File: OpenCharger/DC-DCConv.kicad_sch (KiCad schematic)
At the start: 10 parts, among them Q5 IPT015N10N5, Q6 IPT015N10N5, Q7 IPT015N10N5, Q9 IPT015N10N5, U4 IRS25606S

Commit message: updated
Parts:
- removed C12, C13, C9: 56uF, Capacitor_THT:CP_Radial_D40.0mm_P10.00mm_SnapIn, symbol Device:C_Polarized_US
- removed U4: IRS25606S, Package_SO:SOIC-8_3.9x4.9mm_P1.27mm, symbol Driver_FET:IRS25606S
- added C10, C15, C16, C6, C8: 100uF, Capacitor_THT:CP_Radial_D16.0mm_P7.50mm, symbol Device:C_Polarized_US
- added Q18, Q19, Q20, Q21, Q22, Q23, Q24, Q25: IPT015N10N5, Package_TO_SOT_SMD:Infineon_PG-HSOF-8-1, symbol Transistor_FET:IPT015N10N5
- C14: value 56uF -> 100uF; footprint Capacitor_THT:CP_Radial_D40.0mm_P10.00mm_SnapIn -> Capacitor_THT:CP_Radial_D16.0mm_P7.50mm
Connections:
- net V_{in}-: now also C10.2, C15.2, C16.2, C6.2, C8.2
- net V_{out}+: now also C10.1, C15.1, C16.1, C6.1, C8.1, Q25.3 (D); no longer Q9.3 (D)
- net BOOST_SG0: now reaches Q7.1 (G)
- net L-: now reaches L1.2, Q9.2 (S)
- net L-: now also Q22.3 (D); no longer Q7.3 (D)
- net BUCK_DG0: now reaches Q6.1 (G)
- net BOOST_DG0: now reaches Q9.1 (G)
- net BUCK_SG2: now reaches Q5.1 (G)
- new net BOOST_DG1: Q24.1 (G)
- new net BOOST_DG2: Q25.1 (G)
- new net BOOST_DS1: Q24.2 (S), Q9.3 (D)
- new net BOOST_DS2: Q24.3 (D), Q25.2 (S)
- new net BOOST_SG1: Q23.1 (G)
- new net BOOST_SG2: Q22.1 (G)
- new net BOOST_SS1: Q23.2 (S), Q7.3 (D)
- new net BOOST_SS2: Q22.2 (S), Q23.3 (D)
- new net BUCK_DG1: Q21.1 (G)
- new net BUCK_DG2: Q20.1 (G)
- new net BUCK_DS1: Q21.2 (S), Q6.3 (D)
- new net BUCK_DS2: Q20.2 (S), Q21.3 (D)
- new net BUCK_SG0: Q19.1 (G)
- new net BUCK_SG1: Q18.1 (G)
- new net BUCK_SS1: Q18.2 (S), Q19.3 (D)
- new net BUCK_SS2: Q18.3 (D), Q5.2 (S)
- new net L+: L1.1, Q19.2 (S), Q20.3 (D)
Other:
- added sheet DC-DC Converter Gate Driver (DCDCGateDrivers.kicad_sch)
- moved on the sheet: L1, Q5, Q6, Q7, Q9

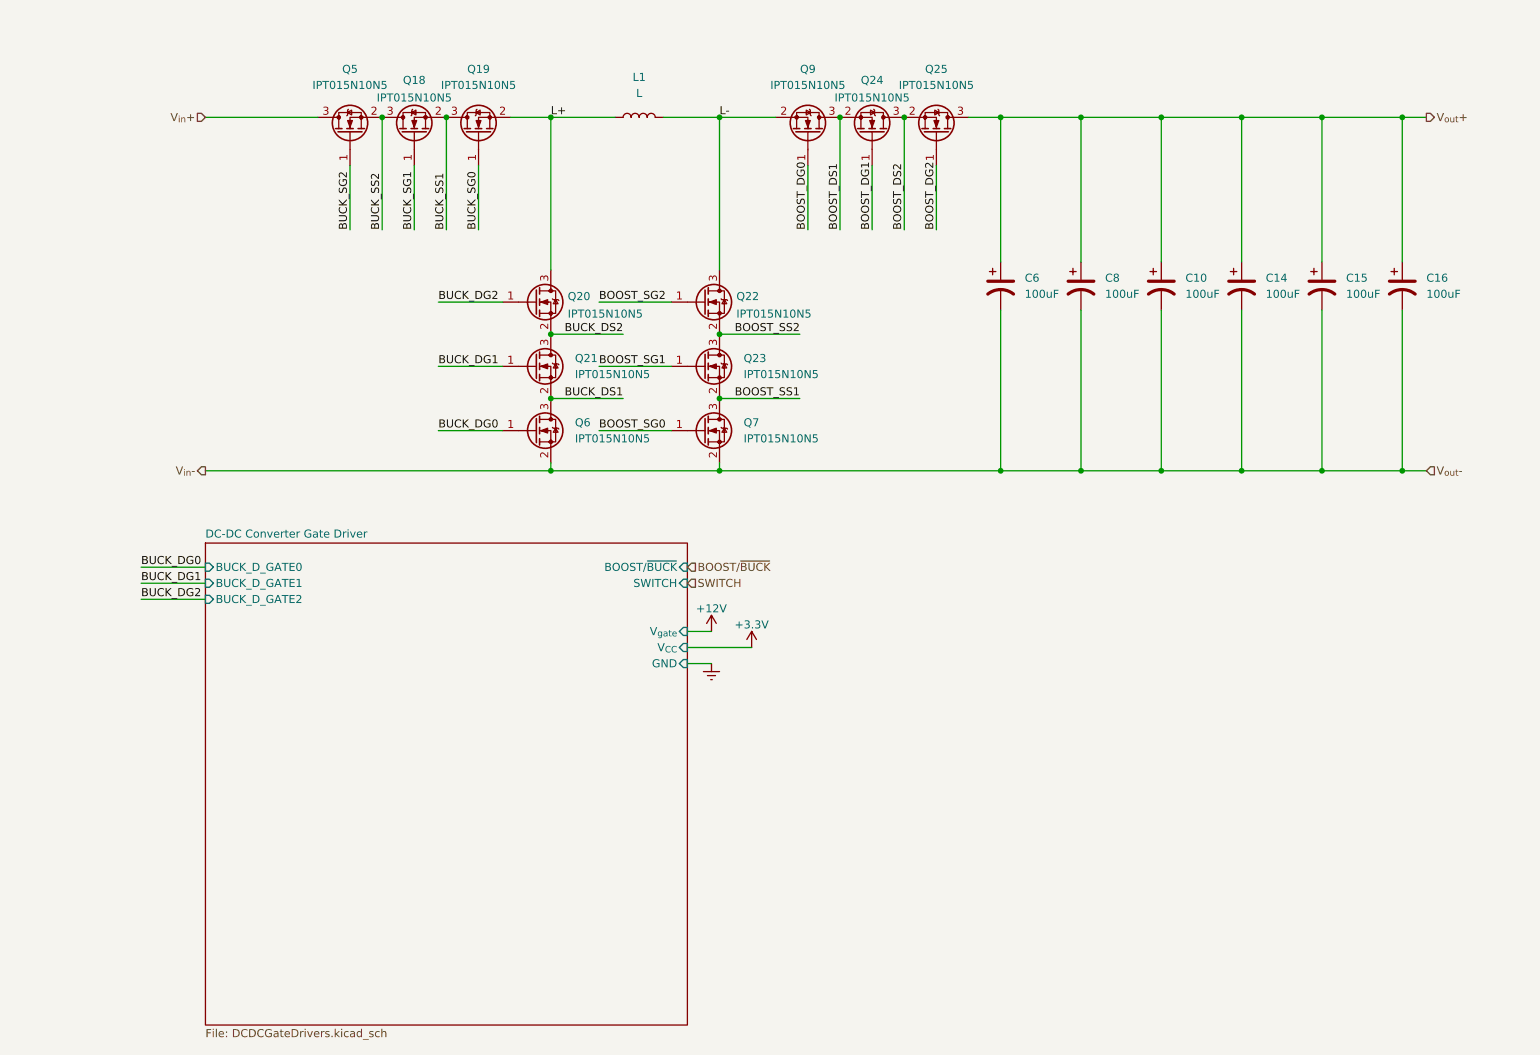
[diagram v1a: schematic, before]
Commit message: Updated Charger and MC
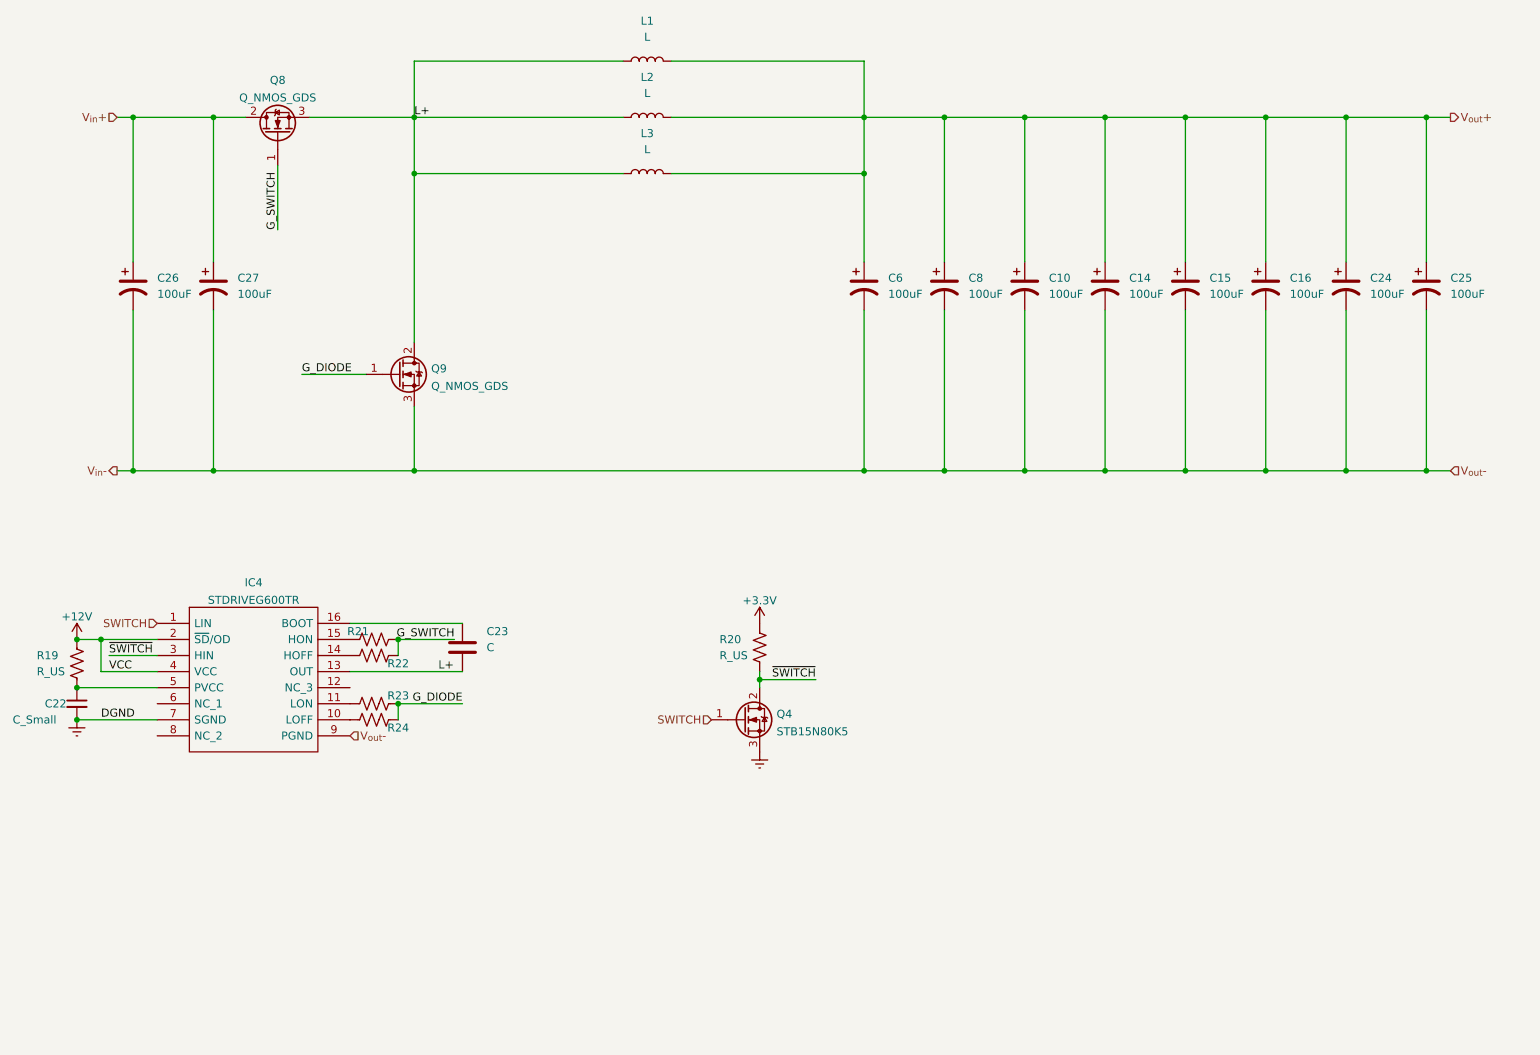
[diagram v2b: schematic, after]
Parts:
- removed Q18, Q19, Q20, Q21, Q22, Q23, Q24, Q25, Q5, Q6, Q7, Q9: IPT015N10N5, Package_TO_SOT_SMD:Infineon_PG-HSOF-8-1, symbol Transistor_FET:IPT015N10N5
- added C22: C_Small, symbol Device:C_Small
- added C23: C, symbol Device:C
- added C24, C25, C26, C27: 100uF, Capacitor_THT:CP_Radial_D16.0mm_P7.50mm, symbol Device:C_Polarized_US
- added IC4: STDRIVEG600TR, SOIC127P600X175-16N, symbol SamacSys_Parts:STDRIVEG600TR
- added L2, L3: L, Inductor_THT:L_Toroid_Vertical_L22.4mm_W10.2mm_P7.90mm_Vishay_TJ4, symbol Device:L
- added Q4: STB15N80K5, Package_TO_SOT_SMD:SOT-23, symbol Transistor_FET:STB15N80K5
- added Q8, Q9: Q_NMOS_GDS, Package_TO_SOT_SMD:TO-263-3_TabPin2, symbol Device:Q_NMOS_GDS
- added R19, R20, R21, R22, R23, R24: R_US, symbol Device:R_US
- L1: footprint Inductor_THT:L_Toroid_Vertical_L67.6mm_W36.1mm_P31.80mm_Vishay_TJ9 -> Inductor_THT:L_Toroid_Vertical_L22.4mm_W10.2mm_P7.90mm_Vishay_TJ4
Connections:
- net L- is gone; now on net V_{out}+: L1.2
- net +12V: now also IC4.2 (~{SD}/OD), IC4.4 (VCC), R19.1
- net +3V3: now also R20.1
- net Earth: now also C22.2, IC4.7 (SGND), Q4.3 (S)
- net L+: now also C23.2, IC4.13 (OUT), L2.1, L3.1, Q8.3 (S), Q9.2 (D)
- net SWITCH: now also IC4.1 (LIN), Q4.1 (G)
- net V_{in}+: now also C26.1, C27.1, Q8.2 (D)
- net V_{in}-: now also C24.2, C25.2, C26.2, C27.2, IC4.9 (PGND), Q9.3 (S)
- net V_{out}+: now also C24.1, C25.1, L2.2, L3.2
- new net: IC4.14 (HOFF), R22.2
- new net: IC4.10 (LOFF), R24.2
- new net: C22.1, IC4.5 (PVCC), R19.2
- new net: C23.1, IC4.16 (BOOT)
- new net: IC4.11 (LON), R23.2
- new net: IC4.15 (HON), R21.2
- new net G_DIODE: Q9.1 (G), R23.1, R24.1
- new net G_SWITCH: Q8.1 (G), R21.1, R22.1
- new net ~{SWITCH}: IC4.3 (HIN), Q4.2 (D), R20.2
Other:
- removed sheet DC-DC Converter Gate Driver
- moved on the sheet: C10, C14, C15, C16, C6, C8
